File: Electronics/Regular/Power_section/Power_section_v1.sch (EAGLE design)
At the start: 14 parts

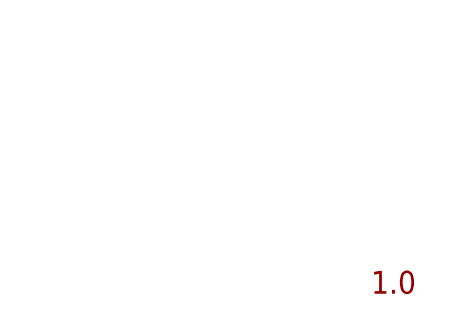
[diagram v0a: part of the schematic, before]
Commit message: Power section improved
What has been improved:
- changed fuse holder slot for the smaller model,
- made wires wider
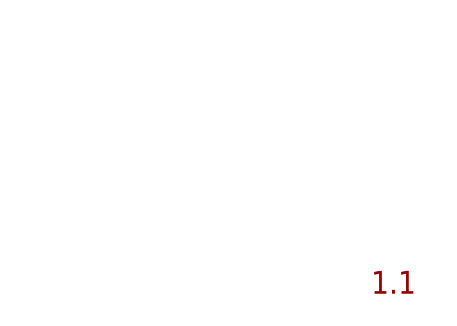
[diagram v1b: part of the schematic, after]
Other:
- note added: "1.1"
- note removed: "1.0"
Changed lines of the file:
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@@
 <text x="175.26" y="27.94" size="2.54" layer="94">Author: sesame0707</text>
 <text x="205.994" y="11.43" size="2.54" layer="94">6</text>
-<text x="261.62" y="7.112" size="2.54" layer="94">1.0</text>
+<text x="261.62" y="7.112" size="2.54" layer="94">1.1</text>
 </plain>
 <instances>

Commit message: Power section improved
What has been improved:
- moved BAT+ and BAT- pads to the very left,
- made wires wider
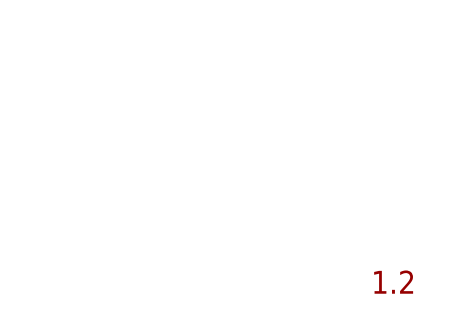
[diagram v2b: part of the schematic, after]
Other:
- note added: "1.2"
- note removed: "1.1"
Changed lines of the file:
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@@
 <text x="175.26" y="27.94" size="2.54" layer="94">Author: sesame0707</text>
 <text x="205.994" y="11.43" size="2.54" layer="94">6</text>
-<text x="261.62" y="7.112" size="2.54" layer="94">1.1</text>
+<text x="261.62" y="7.112" size="2.54" layer="94">1.2</text>
 </plain>
 <instances>
